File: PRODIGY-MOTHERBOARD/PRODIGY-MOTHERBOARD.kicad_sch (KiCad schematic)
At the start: 0 parts

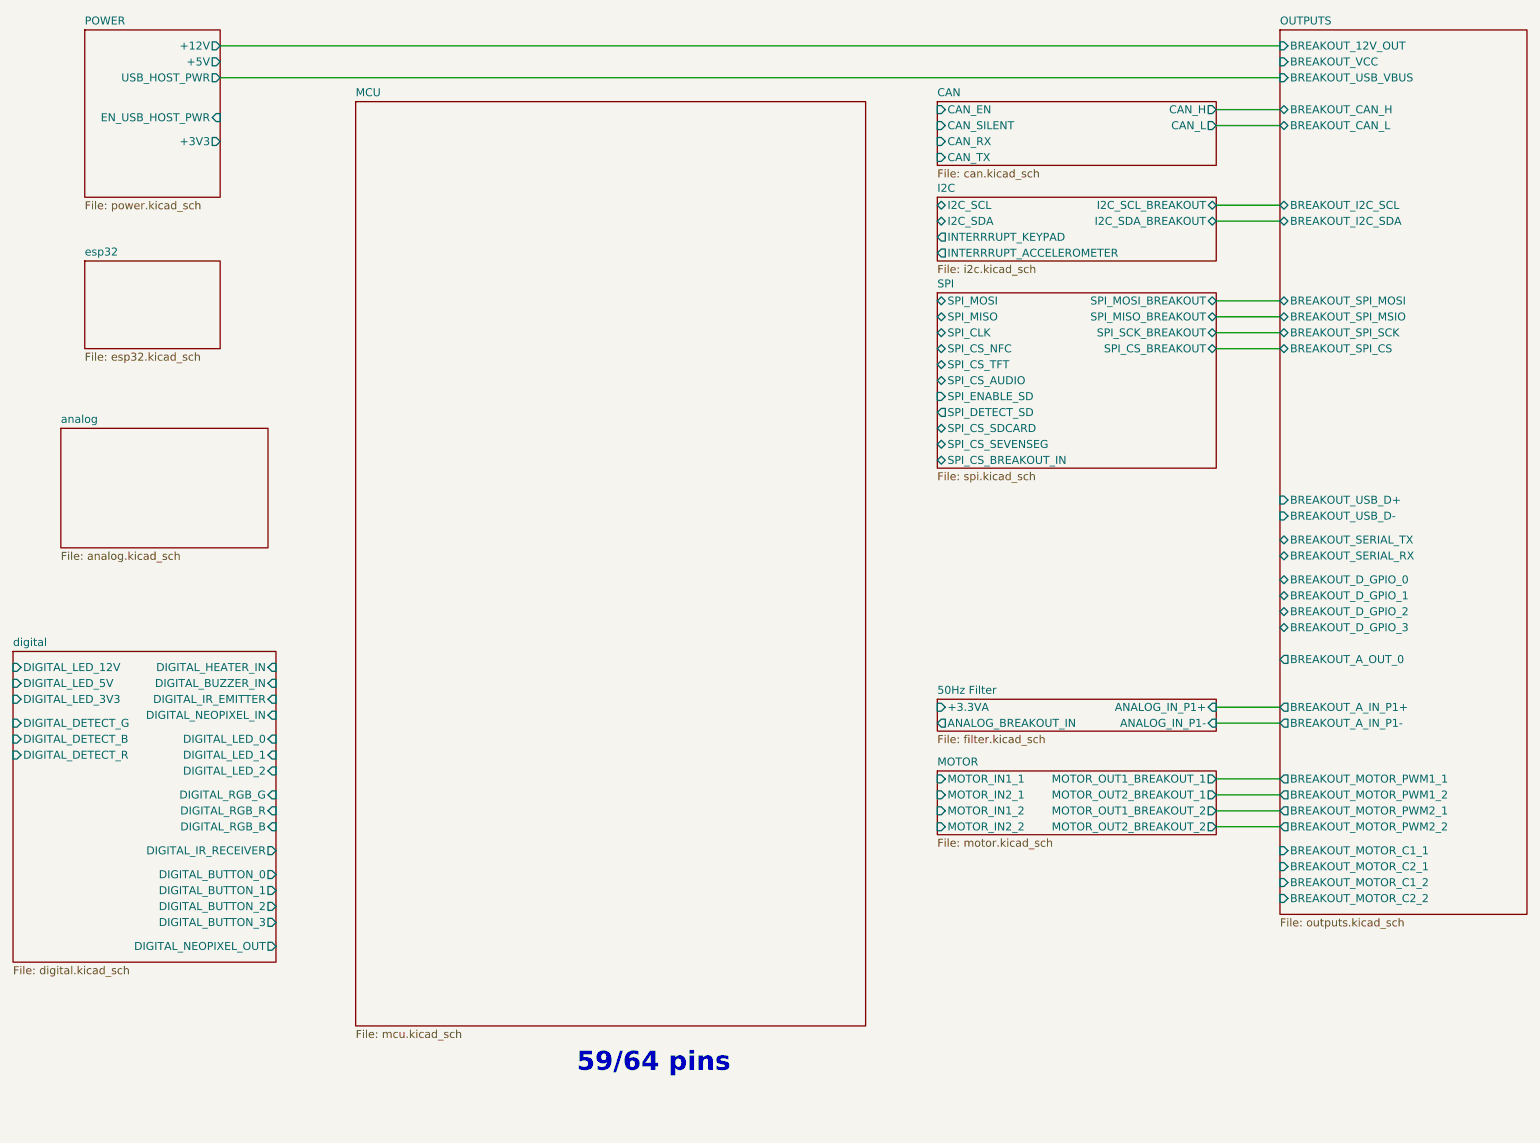
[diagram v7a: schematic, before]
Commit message: Analog schematic finished, except the joystick part.
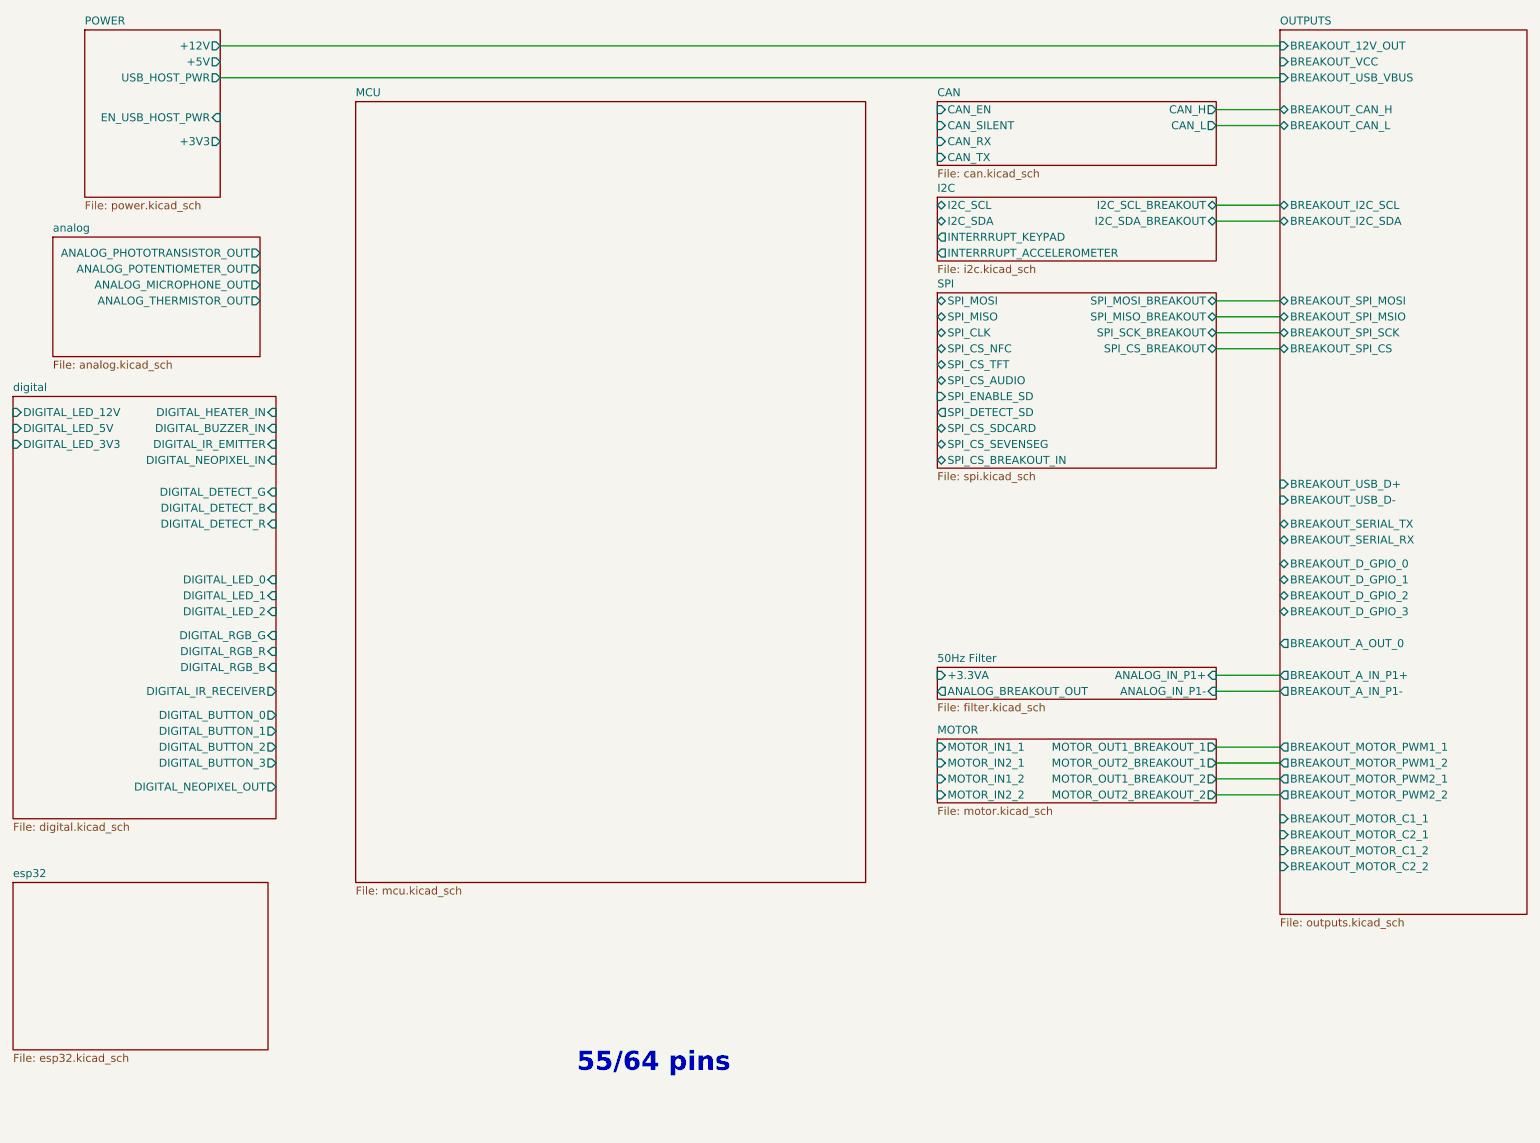
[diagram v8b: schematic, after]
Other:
- sheet 50Hz Filter ports: added ANALOG_BREAKOUT_OUT; removed ANALOG_BREAKOUT_IN
- sheet analog ports: added ANALOG_MICROPHONE_OUT, ANALOG_PHOTOTRANSISTOR_OUT, ANALOG_POTENTIOMETER_OUT, ANALOG_THERMISTOR_OUT; removed none
- note added: "55/64 pins"
- note removed: "59/64 pins"
